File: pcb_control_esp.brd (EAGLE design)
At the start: 100 x 50 mm, 45 parts, among them IC1 AT24CP, IC2 REG1117, IC4 DS3231SN, IC5 74LS595N, K1 HKE, Q1 BC337, Q2 BC337, X1 VIN

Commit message: finish
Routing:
- net VCC: track 131.3 -> 132.0 mm
- net RST: track 41.5 -> 40.7 mm
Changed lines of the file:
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@@
 <layer number="23" name="tOrigins" color="15" fill="1" visible="yes" active="yes"/>
 <layer number="24" name="bOrigins" color="15" fill="1" visible="yes" active="yes"/>
-<layer number="25" name="tNames" color="7" fill="1" visible="yes" active="yes"/>
-<layer number="26" name="bNames" color="7" fill="1" visible="yes" active="yes"/>
+<layer number="25" name="tNames" color="7" fill="1" visible="no" active="yes"/>
+<layer number="26" name="bNames" color="7" fill="1" visible="no" active="yes"/>
 <layer number="27" name="tValues" color="7" fill="1" visible="yes" active="yes"/>
 <layer number="28" name="bValues" color="7" fill="1" visible="yes" active="yes"/>
@@
 <wire x1="46.99" y1="18.415" x2="45.72" y2="19.685" width="0.6096" layer="1"/>
 <wire x1="45.72" y1="19.685" x2="40.64" y2="19.685" width="0.6096" layer="1"/>
-<wire x1="35.56" y1="34.925" x2="40.64" y2="29.845" width="0.4064" layer="16"/>
-<wire x1="40.64" y1="29.845" x2="40.64" y2="19.685" width="0.4064" layer="16"/>
+<wire x1="35.56" y1="34.925" x2="36.83" y2="34.925" width="0.4064" layer="16"/>
+<wire x1="36.83" y1="34.925" x2="37.465" y2="34.29" width="0.4064" layer="16"/>
+<wire x1="37.465" y1="34.29" x2="37.465" y2="30.48" width="0.4064" layer="16"/>
+<wire x1="37.465" y1="30.48" x2="40.64" y2="27.305" width="0.4064" layer="16"/>
+<wire x1="40.64" y1="27.305" x2="40.64" y2="19.685" width="0.4064" layer="16"/>
 <wire x1="63.5" y1="29.21" x2="58.42" y2="29.21" width="0.4064" layer="16"/>
 <wire x1="58.42" y1="29.21" x2="57.15" y2="27.94" width="0.4064" layer="16"/>
@@
 <wire x1="35.56" y1="45.085" x2="36.83" y2="45.085" width="0.4064" layer="16"/>
 <wire x1="36.83" y1="45.085" x2="37.465" y2="44.45" width="0.4064" layer="16"/>
-<wire x1="37.465" y1="44.45" x2="37.465" y2="40.005" width="0.4064" layer="16"/>
-<wire x1="37.465" y1="40.005" x2="38.735" y2="38.735" width="0.4064" layer="16"/>
-<wire x1="38.735" y1="38.735" x2="38.735" y2="34.29" width="0.4064" layer="16"/>
-<wire x1="38.735" y1="34.29" x2="41.275" y2="31.75" width="0.4064" layer="16"/>
-<wire x1="41.275" y1="31.75" x2="45.72" y2="31.75" width="0.4064" layer="16"/>
-<wire x1="45.72" y1="31.75" x2="46.99" y2="30.48" width="0.4064" layer="16"/>
-<wire x1="46.99" y1="30.48" x2="46.99" y2="26.035" width="0.4064" layer="16"/>
+<wire x1="37.465" y1="44.45" x2="37.465" y2="40.64" width="0.4064" layer="16"/>
+<wire x1="37.465" y1="40.64" x2="38.1" y2="40.005" width="0.4064" layer="16"/>
+<wire x1="38.1" y1="40.005" x2="41.275" y2="40.005" width="0.4064" layer="16"/>
+<wire x1="41.275" y1="40.005" x2="43.18" y2="38.1" width="0.4064" layer="16"/>
+<wire x1="43.18" y1="38.1" x2="43.18" y2="34.925" width="0.4064" layer="16"/>
+<wire x1="43.18" y1="34.925" x2="46.99" y2="31.115" width="0.4064" layer="16"/>
+<wire x1="46.99" y1="31.115" x2="46.99" y2="26.035" width="0.4064" layer="16"/>
 </signal>
 <signal name="N$4">

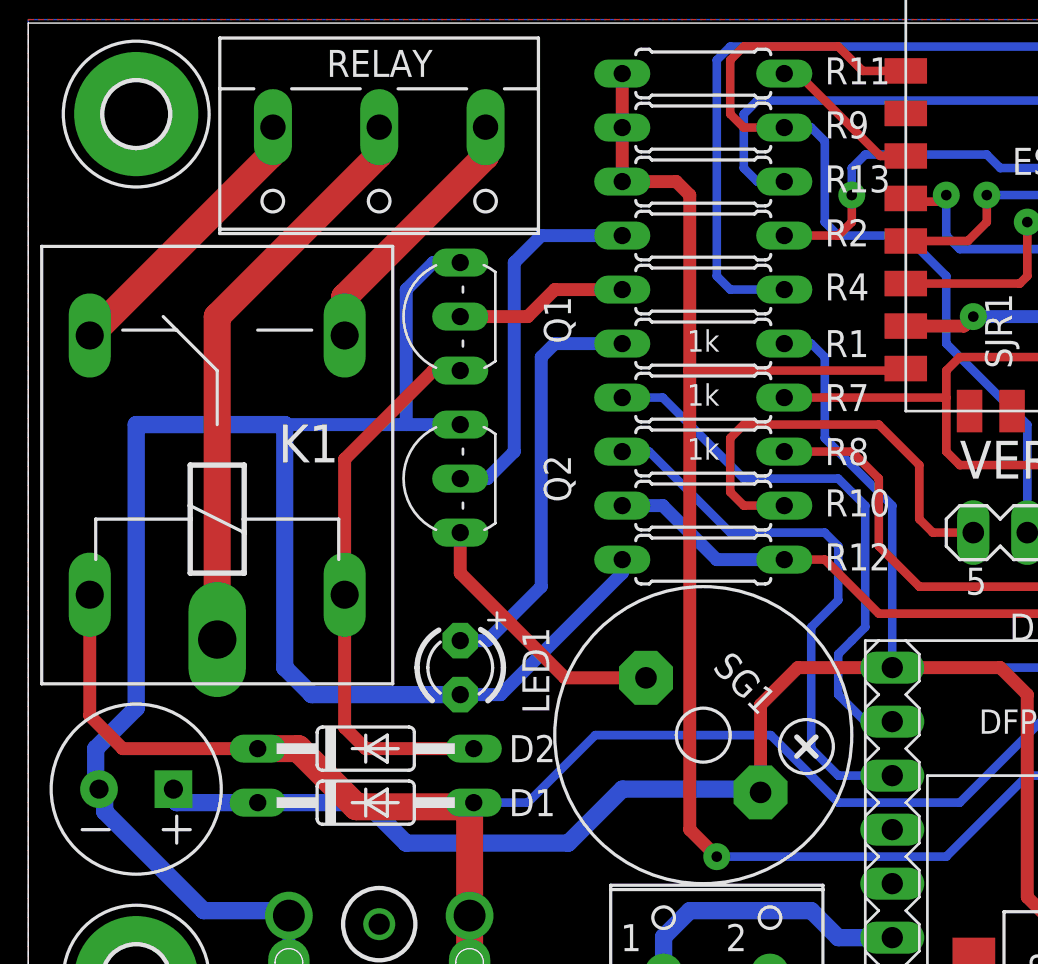
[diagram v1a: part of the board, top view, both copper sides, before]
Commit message: pindah jalur downloader
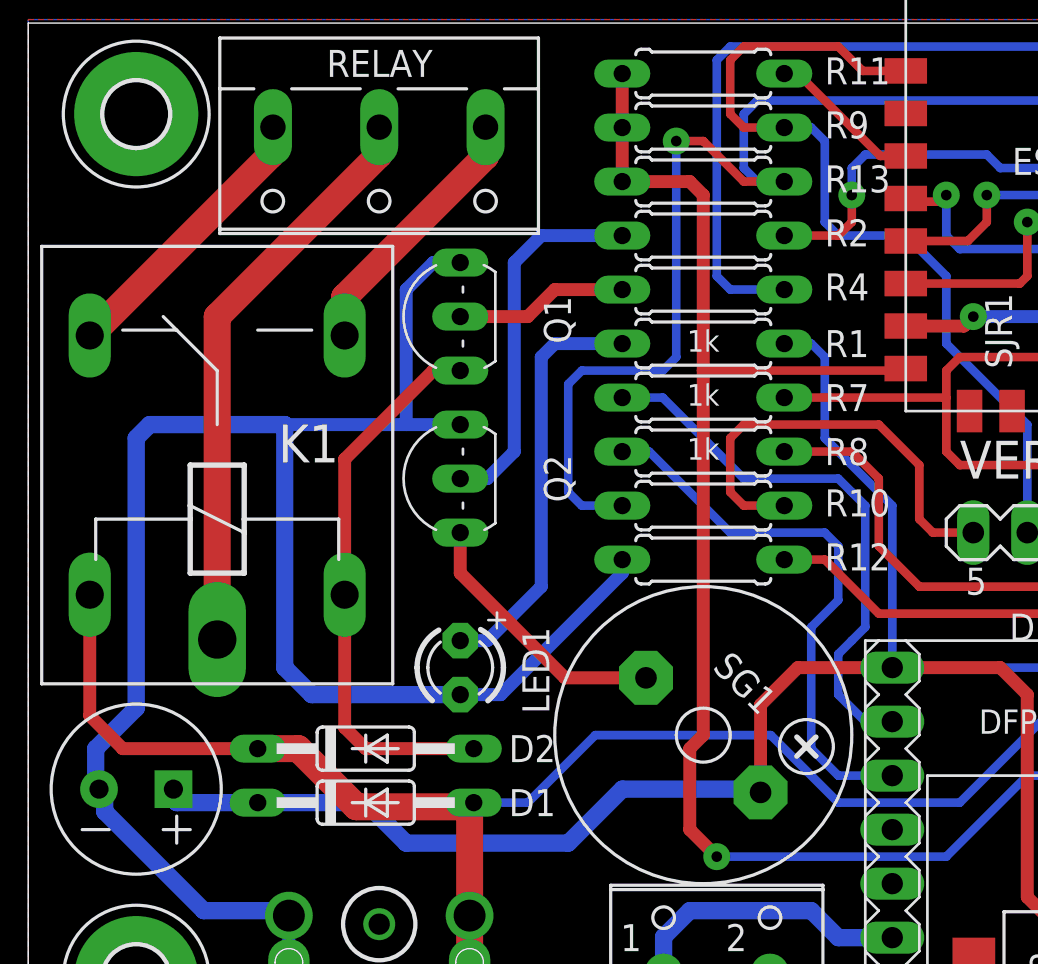
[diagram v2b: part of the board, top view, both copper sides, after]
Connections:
- net CLK: now also R10.2
- net STB: no longer R10.2
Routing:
- net CLK: track 95.0 -> 124.5 mm, vias 1 -> 2
- net STB: track 123.0 -> 114.4 mm
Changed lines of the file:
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@@
 <grid distance="0.025" unitdist="inch" unit="mm" style="lines" multiple="1" display="yes" altdistance="0.025" altunitdist="inch" altunit="inch"/>
 <layers>
-<layer number="1" name="Top" color="4" fill="1" visible="yes" active="yes"/>
+<layer number="1" name="Top" color="4" fill="1" visible="no" active="yes"/>
 <layer number="2" name="Route2" color="1" fill="3" visible="no" active="no"/>
 <layer number="3" name="Route3" color="4" fill="3" visible="no" active="no"/>
@@
 <wire x1="13.335" y1="18.415" x2="12.065" y2="19.685" width="0.8128" layer="16"/>
 <wire x1="12.065" y1="19.685" x2="12.065" y2="31.115" width="0.8128" layer="16"/>
-<wire x1="12.065" y1="31.115" x2="5.08" y2="31.115" width="0.8128" layer="16"/>
-<wire x1="5.08" y1="31.115" x2="5.08" y2="17.78" width="0.8128" layer="16"/>
+<wire x1="12.065" y1="31.115" x2="5.715" y2="31.115" width="0.8128" layer="16"/>
+<wire x1="5.715" y1="31.115" x2="5.08" y2="30.48" width="0.8128" layer="16"/>
+<wire x1="5.08" y1="30.48" x2="5.08" y2="17.78" width="0.8128" layer="16"/>
 <wire x1="5.08" y1="17.78" x2="3.175" y2="15.875" width="0.8128" layer="16"/>
 <wire x1="3.175" y1="15.875" x2="3.175" y2="14.125" width="0.8128" layer="16"/>
@@
 <wire x1="52.705" y1="40.64" x2="52.705" y2="46.355" width="0.4064" layer="1"/>
 <via x="52.705" y="46.355" extent="1-16" drill="0.5" diameter="1.27"/>
+<contactref element="R10" pad="2"/>
+<wire x1="27.94" y1="27.305" x2="26.035" y2="27.305" width="0.4064" layer="16"/>
+<wire x1="26.035" y1="27.305" x2="25.4" y2="27.94" width="0.4064" layer="16"/>
+<wire x1="25.4" y1="27.94" x2="25.4" y2="33.02" width="0.4064" layer="16"/>
+<wire x1="25.4" y1="33.02" x2="26.035" y2="33.655" width="0.4064" layer="16"/>
+<wire x1="26.035" y1="33.655" x2="29.845" y2="33.655" width="0.4064" layer="16"/>
+<wire x1="29.845" y1="33.655" x2="30.48" y2="34.29" width="0.4064" layer="16"/>
+<wire x1="30.48" y1="34.29" x2="30.48" y2="44.45" width="0.4064" layer="16"/>
+<via x="30.48" y="44.45" extent="1-16" drill="0.5" diameter="1.27"/>
+<wire x1="30.48" y1="44.45" x2="31.75" y2="44.45" width="0.4064" layer="1"/>
+<wire x1="31.75" y1="44.45" x2="33.655" y2="42.545" width="0.4064" layer="1"/>
+<wire x1="33.655" y1="42.545" x2="35.56" y2="42.545" width="0.4064" layer="1"/>
 </signal>
 <signal name="VSEG">
@@
 <wire x1="50.7746" y1="5.1054" x2="53.9496" y2="5.1054" width="0.6096" layer="1"/>
 <wire x1="53.9496" y1="5.1054" x2="53.975" y2="5.08" width="0.6096" layer="1"/>
-<wire x1="30.48" y1="42.545" x2="27.94" y2="42.545" width="0.6096" layer="1"/>
+<wire x1="31.115" y1="42.545" x2="27.94" y2="42.545" width="0.6096" layer="1"/>
 <wire x1="27.94" y1="42.545" x2="27.94" y2="45.085" width="0.6096" layer="1"/>
 <wire x1="27.94" y1="45.085" x2="27.94" y2="47.625" width="0.6096" layer="1"/>
 <wire x1="41.275" y1="33.75" x2="41.275" y2="33.655" width="0.4064" layer="1"/>
-<wire x1="41.275" y1="33.655" x2="31.435" y2="33.655" width="0.4064" layer="1"/>
+<wire x1="41.275" y1="33.655" x2="32.07" y2="33.655" width="0.4064" layer="1"/>
 <wire x1="63.5" y1="21.59" x2="56.515" y2="21.59" width="0.4064" layer="16"/>
 <wire x1="56.515" y1="21.59" x2="51.435" y2="16.51" width="0.4064" layer="16"/>
@@
 <wire x1="43.18" y1="10.795" x2="32.385" y2="10.795" width="0.4064" layer="16"/>
 <via x="32.385" y="10.795" extent="1-16" drill="0.5" diameter="1.27"/>
-<wire x1="30.48" y1="42.545" x2="31.115" y2="41.91" width="0.6096" layer="1"/>
-<wire x1="31.115" y1="41.91" x2="31.115" y2="33.655" width="0.6096" layer="1"/>
-<wire x1="31.115" y1="33.655" x2="31.115" y2="12.065" width="0.6096" layer="1"/>
+<wire x1="31.115" y1="42.545" x2="31.75" y2="41.91" width="0.6096" layer="1"/>
+<wire x1="31.75" y1="41.91" x2="31.75" y2="33.655" width="0.6096" layer="1"/>
+<wire x1="31.75" y1="33.655" x2="31.75" y2="16.51" width="0.6096" layer="1"/>
+<wire x1="31.75" y1="16.51" x2="31.115" y2="15.875" width="0.6096" layer="1"/>
+<wire x1="31.115" y1="15.875" x2="31.115" y2="12.065" width="0.6096" layer="1"/>
 <wire x1="31.115" y1="12.065" x2="32.385" y2="10.795" width="0.6096" layer="1"/>
-<wire x1="31.435" y1="33.655" x2="31.115" y2="33.655" width="0.6096" layer="1"/>
+<wire x1="32.07" y1="33.655" x2="31.75" y2="33.655" width="0.6096" layer="1"/>
 <wire x1="77.6" y1="8.8" x2="77.6" y2="11.3" width="0.4064" layer="16"/>
 <wire x1="77.6" y1="11.3" x2="77.47" y2="11.43" width="0.4064" layer="16"/>
@@
 <contactref element="R12" pad="2"/>
 <contactref element="SV2" pad="8"/>
-<contactref element="R10" pad="2"/>
 <wire x1="93.98" y1="36.83" x2="94.615" y2="36.83" width="0.4064" layer="1"/>
 <wire x1="94.615" y1="36.83" x2="95.25" y2="36.195" width="0.4064" layer="1"/>
@@
 <wire x1="94.615" y1="27.94" x2="85.725" y2="27.94" width="0.4064" layer="1"/>
 <wire x1="85.725" y1="27.94" x2="83.185" y2="26.035" width="0.4064" layer="1"/>
-<wire x1="27.94" y1="27.305" x2="29.845" y2="27.305" width="0.6096" layer="16"/>
-<wire x1="29.845" y1="27.305" x2="32.385" y2="24.765" width="0.6096" layer="16"/>
-<wire x1="32.385" y1="24.765" x2="35.56" y2="24.765" width="0.6096" layer="16"/>
 <wire x1="57.475" y1="35.75" x2="56.705" y2="35.75" width="0.4064" layer="1"/>
 <wire x1="56.705" y1="35.75" x2="55.88" y2="34.925" width="0.4064" layer="1"/>
